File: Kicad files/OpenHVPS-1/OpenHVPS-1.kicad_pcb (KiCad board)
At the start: 2 copper layers, 77.5 x 20.5 mm, 71 parts, among them J1 Conn_01x03_Male, J2 Conn_01x03_Male, Q1 FQT7N10, Q2 BC846, Q3 MMDT3906, U1 74HC14, U2 MAX4162, U3 CD14538BM, U4 MAX6008AEUR+T

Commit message: cd \Users\allan\OneDrive\Documents\OpenHVPS  Please enter the commit message for your changes. Lines starting updated the long board design
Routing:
- net +3V3: track 0.00 -> 108.9 mm, vias 0 -> 2
- net Net-(Q1-Pad2): track 0.00 -> 57.3 mm, vias 0 -> 2
- net Net-(C14-Pad1): track 0.00 -> 53.8 mm, vias 0 -> 2
- net Net-(C16-Pad1): track 0.00 -> 49.5 mm, vias 0 -> 2
- net Net-(C19-Pad1): track 0.00 -> 47.4 mm, vias 0 -> 2
- net GND: track 0.00 -> 45.9 mm
- net Net-(H2-Pad1): track 0.00 -> 37.1 mm, vias 0 -> 1
- net Net-(Q2-Pad1): track 0.00 -> 32.8 mm, vias 0 -> 2
- net Net-(D9-Pad2): track 0.00 -> 32.4 mm
- net Net-(Q3-Pad1): track 0.00 -> 28.1 mm, vias 0 -> 2
- net Net-(C21-Pad1): track 0.00 -> 27.9 mm, vias 0 -> 3
- net Net-(D9-Pad1): track 0.00 -> 23.2 mm, vias 0 -> 2
- net Net-(D8-Pad2): track 0.00 -> 22.8 mm, vias 0 -> 2
- net Net-(C15-Pad1): track 0.00 -> 22.8 mm, vias 0 -> 2
- net +2V5: track 0.00 -> 22.6 mm, vias 0 -> 3
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
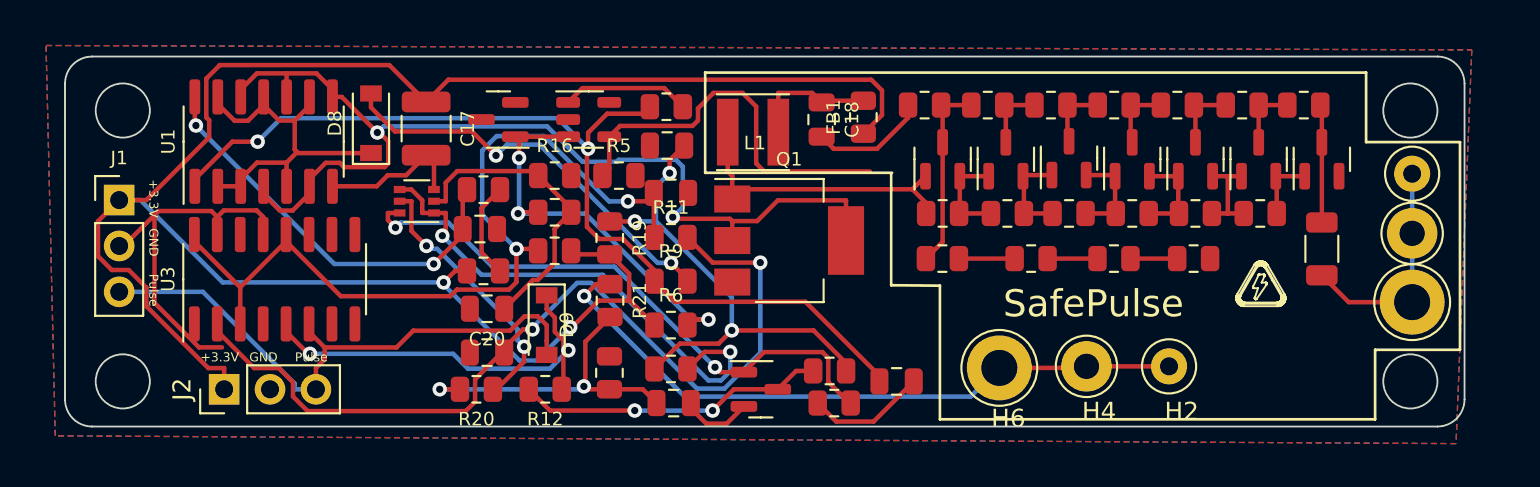
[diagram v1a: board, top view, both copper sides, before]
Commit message: changes to anode and cathode plus some parts layout, not routed!
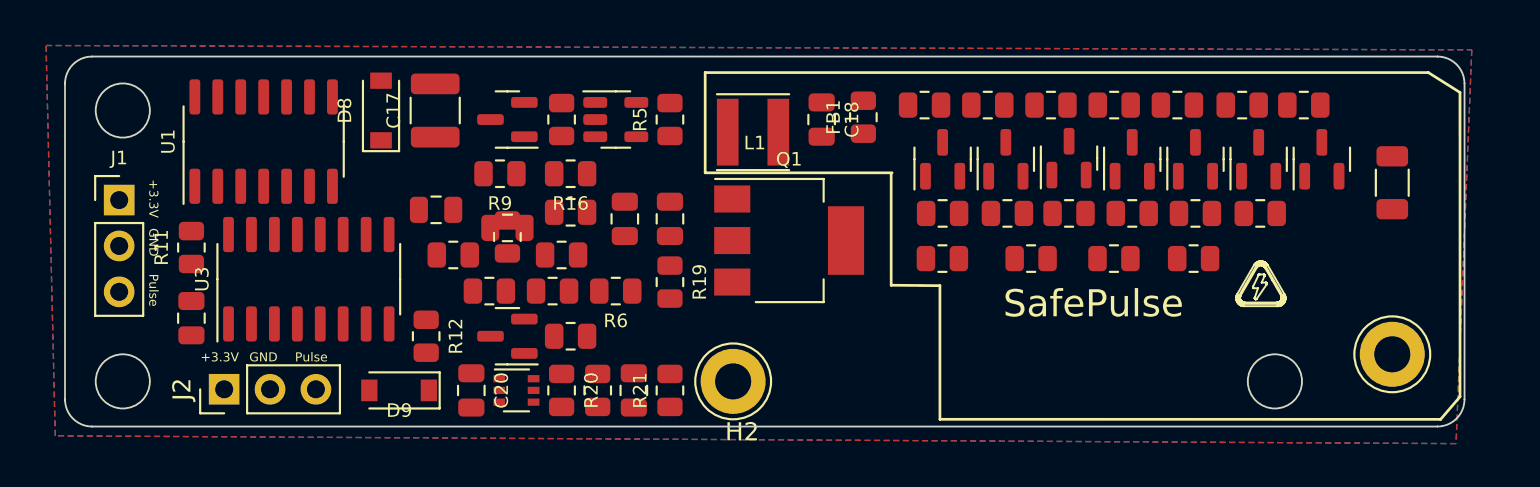
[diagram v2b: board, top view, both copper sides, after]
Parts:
- removed H1: A-1, TestPoint:TestPoint_Loop_D1.80mm_Drill1.0mm_Beaded
- removed H3: A-2, TestPoint:TestPoint_Loop_D2.60mm_Drill1.4mm_Beaded
- removed H4: C-2, TestPoint:TestPoint_Loop_D2.60mm_Drill1.4mm_Beaded
- removed H6: C-3, TestPoint:TestPoint_Loop_D3.80mm_Drill2.0mm
- H2: value C-1 -> Cathode; footprint TestPoint:TestPoint_Loop_D1.80mm_Drill1.0mm_Beaded -> TestPoint:TestPoint_Loop_D3.80mm_Drill2.0mm
- H5: value A-3 -> Anode
- moved R11 26.6 mm to (97.5, 67.6), turned to 90 degrees
- moved H2 24.2 mm to (127.5, 75.0)
- moved C14 23.2 mm to (115.0, 66.5)
- moved R14 21.8 mm to (112.0, 68.0)
- moved C16 16.5 mm to (97.5, 71.5), turned to -90 degrees
- moved R17 15.1 mm to (118.5, 72.5), turned to 0 degrees
- moved Q2 14.3 mm to (115.0, 72.5), turned to 180 degrees
- moved Q3 11.8 mm to (115.5, 75.5), turned to 0 degrees
- moved R9 11.2 mm to (114.6, 63.5), turned to 180 degrees
- moved R18 10.9 mm to (114.0, 70.0)
- moved D9 8.94 mm to (109.0, 75.5), turned to 180 degrees
- moved R12 7.22 mm to (110.5, 72.5), turned to -90 degrees
- moved R21 5.98 mm to (124.0, 75.5), turned to 90 degrees
- moved R8 5.84 mm to (118.0, 60.5), turned to 90 degrees
- moved R7 5.35 mm to (164.0, 64.0)
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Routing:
- net +3V3: track 108.9 -> 0.00 mm, vias 2 -> 0
- net Net-(Q1-Pad2): track 57.3 -> 0.00 mm, vias 2 -> 0
- net Net-(C14-Pad1): track 53.8 -> 0.00 mm, vias 2 -> 0
- net Net-(C16-Pad1): track 49.5 -> 0.00 mm, vias 2 -> 0
- net Net-(C19-Pad1): track 47.4 -> 0.00 mm, vias 2 -> 0
- net GND: track 45.9 -> 0.00 mm
- net Net-(H2-Pad1): track 37.1 -> 0.00 mm, vias 1 -> 0
- net Net-(Q2-Pad1): track 32.8 -> 0.00 mm, vias 2 -> 0
- net Net-(D9-Pad2): track 32.4 -> 0.00 mm
- net Net-(Q3-Pad1): track 28.1 -> 0.00 mm, vias 2 -> 0
- net Net-(C21-Pad1): track 27.9 -> 0.00 mm, vias 3 -> 0
- net Net-(D9-Pad1): track 23.2 -> 0.00 mm, vias 2 -> 0
- net Net-(D8-Pad2): track 22.8 -> 0.00 mm, vias 2 -> 0
- net Net-(C15-Pad1): track 22.8 -> 0.00 mm, vias 2 -> 0
- net +2V5: track 22.6 -> 0.00 mm, vias 3 -> 0
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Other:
- outline, holes or cut-outs redrawn

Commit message: Routed the board
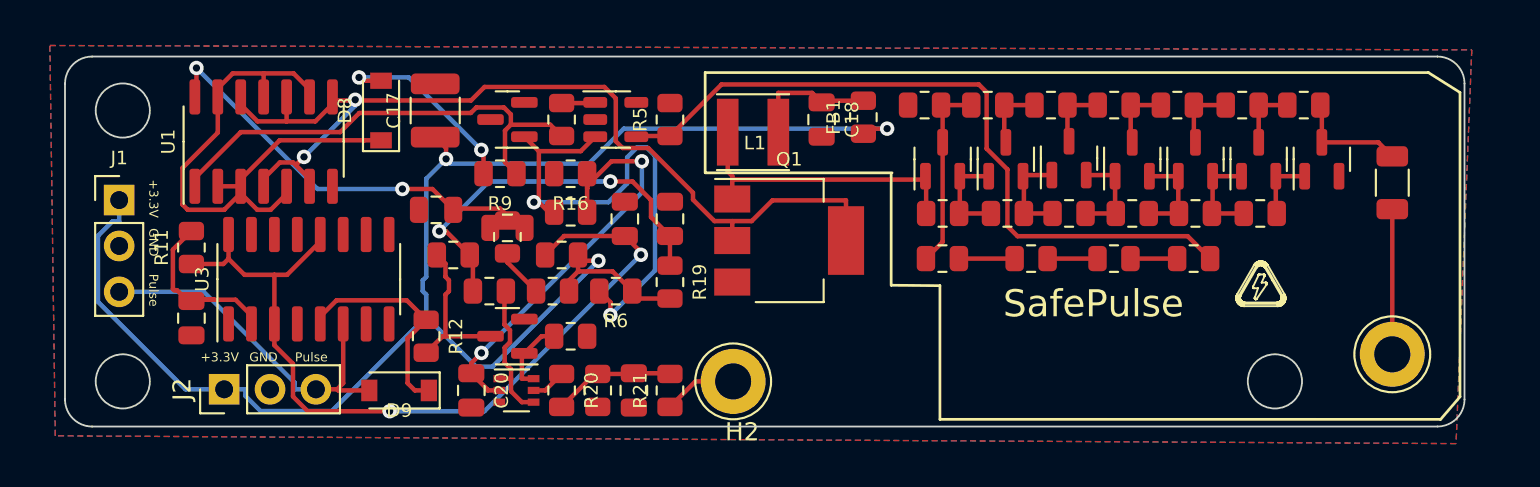
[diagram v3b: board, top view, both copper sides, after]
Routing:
- net +3V3: track 0.00 -> 89.1 mm, vias 0 -> 3
- net Net-(Q1-Pad2): track 0.00 -> 54.4 mm, vias 0 -> 2
- net Net-(C19-Pad1): track 0.00 -> 46.7 mm, vias 0 -> 2
- net Net-(R4-Pad1): track 0.00 -> 40.6 mm
- net Net-(D8-Pad1): track 0.00 -> 32.9 mm
- net +2V5: track 0.00 -> 29.2 mm, vias 0 -> 2
- net Net-(C14-Pad1): track 0.00 -> 26.5 mm
- net Net-(C20-Pad1): track 0.00 -> 23.5 mm, vias 0 -> 2
- net Net-(C15-Pad1): track 0.00 -> 22.6 mm, vias 0 -> 2
- net Net-(C21-Pad1): track 0.00 -> 21.7 mm, vias 0 -> 2
- net Net-(D9-Pad2): track 0.00 -> 20.1 mm
- net Net-(C2-Pad1): track 0.00 -> 16.5 mm
- net Net-(D9-Pad1): track 0.00 -> 12.4 mm
- net Net-(D8-Pad2): track 0.00 -> 11.1 mm, vias 0 -> 2
- net Net-(C1-Pad2): track 0.00 -> 10.6 mm
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
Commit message: Changed foot prints for Anade/Cathode
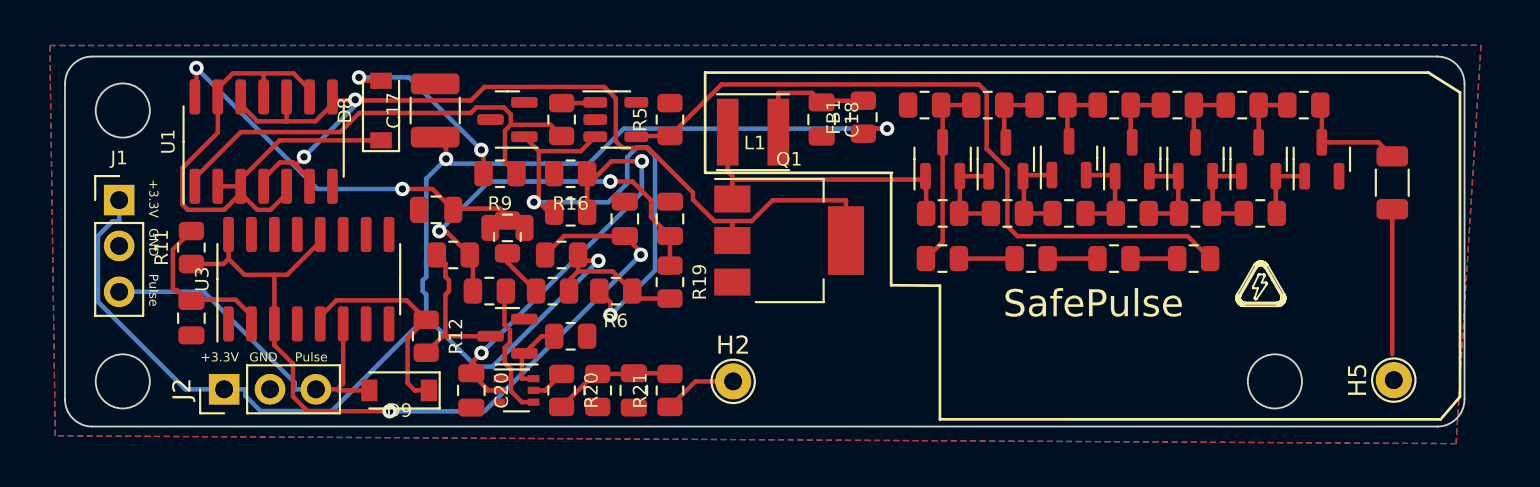
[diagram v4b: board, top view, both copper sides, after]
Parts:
- H2, H5: footprint TestPoint:TestPoint_Loop_D3.80mm_Drill2.0mm -> TestPoint:TestPoint_THTPad_D2.0mm_Drill1.0mm
- moved H5 1.43 mm to (164.1, 74.9)
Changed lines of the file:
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@@
       (net 24 "Net-(D9-Pad2)") (pinfunction "Pin_3"))
     (model "${KICAD6_3DMODEL_DIR}/Connector_PinHeader_2.54mm.3dshapes/PinHeader_1x03_P2.54mm_Vertical.wrl"
-      (offset (xyz 0 0 0))
+      (offset (xyz 0 0 -2))
       (scale (xyz 1 1 1))
-      (rotate (xyz 0 0 0))
+      (rotate (xyz 0 -180 0))
     )
   )
-  (footprint "TestPoint:TestPoint_Loop_D3.80mm_Drill2.0mm" (layer "F.Cu")
-    (at 164 73.5 90)
-    (descr "wire loop as test point, loop diameter 3.8mm, hole diameter 2.0mm")
-    (tags "test point wire loop bead")
+  (footprint "TestPoint:TestPoint_THTPad_D2.0mm_Drill1.0mm" (layer "F.Cu")
+    (at 164.084 74.93 90)
+    (descr "THT pad as test Point, diameter 2.0mm, hole diameter 1.0mm")
+    (tags "test point THT pad")
     (property "Sheet file" "OpenHVPS-1.kicad_sch")
     (property "Sheet name" "")
-    (attr through_hole)
-    (fp_text reference "H5" (at 0.5 2.8 90) (layer "F.SilkS") hide
+    (attr exclude_from_pos_files exclude_from_bom)
+    (fp_text reference "H5" (at 0 -1.998 90) (layer "F.SilkS")
       (effects (font (size 1 1) (thickness 0.15)))
     )
-    (fp_text value "Anode" (at 0 -2.8 90) (layer "F.Fab")
+    (fp_text value "Anode" (at 0 2.05 90) (layer "F.Fab")
       (effects (font (size 1 1) (thickness 0.15)))
     )
-    (fp_text user "${REFERENCE}" (at 0.5 2.8 90) (layer "F.Fab") hide
+    (fp_text user "${REFERENCE}" (at 0 -2 90) (layer "F.Fab")
       (effects (font (size 1 1) (thickness 0.15)))
     )
-    (fp_circle (center 0 0) (end 2.1 0) (layer "F.SilkS") (width 0.12) (fill none))
-    (fp_circle (center 0 0) (end 2.3 0) (layer "F.CrtYd") (width 0.05) (fill none))
-    (fp_line (start 1.9 0.3) (end 1.9 -0.3) (layer "F.Fab") (width 0.12))
-    (fp_line (start 1.9 -0.3) (end -1.9 -0.3) (layer "F.Fab") (width 0.12))
-    (fp_line (start -1.9 -0.3) (end -1.9 0.3) (layer "F.Fab") (width 0.12))
-    (fp_line (start -1.9 0.3) (end 1.9 0.3) (layer "F.Fab") (width 0.12))
-    (pad "1" thru_hole circle (at 0 0 90) (locked) (size 3.6 3.6) (drill 2) (layers *.Cu *.Mask)
+    (fp_circle (center 0 0) (end 0 1.2) (layer "F.SilkS") (width 0.12) (fill none))
+    (fp_circle (center 0 0) (end 1.5 0) (layer "F.CrtYd") (width 0.05) (fill none))
+    (pad "1" thru_hole circle (at 0 0 90) (locked) (size 2 2) (drill 1) (layers *.Cu *.Mask)
       (net 49 "Net-(H5-Pad1)") (pinfunction "1"))
-    (model "${KICAD6_3DMODEL_DIR}/TestPoint.3dshapes/TestPoint_Loop_D3.80mm_Drill2.0mm.wrl"
-      (offset (xyz 0 0 0))
-      (scale (xyz 1 1 1))
-      (rotate (xyz 0 0 0))
-    )
   )
   (footprint "Package_TO_SOT_SMD:SOT-23" (layer "F.Cu")
@@
     )
   )
-  (footprint "TestPoint:TestPoint_Loop_D3.80mm_Drill2.0mm" (layer "F.Cu")
+  (footprint "TestPoint:TestPoint_THTPad_D2.0mm_Drill1.0mm" (layer "F.Cu")
     (at 127.5 75)
-    (descr "wire loop as test point, loop diameter 3.8mm, hole diameter 2.0mm")
-    (tags "test point wire loop bead")
+    (descr "THT pad as test Point, diameter 2.0mm, hole diameter 1.0mm")
+    (tags "test point THT pad")
     (property "Sheet file" "OpenHVPS-1.kicad_sch")
     (property "Sheet name" "")
-    (attr through_hole)
-    (fp_text reference "H2" (at 0.5 2.8) (layer "F.SilkS")
+    (attr exclude_from_pos_files exclude_from_bom)
+    (fp_text reference "H2" (at 0 -1.998) (layer "F.SilkS")
       (effects (font (size 1 1) (thickness 0.15)))
     )
-    (fp_text value "Cathode" (at 0 -2.8) (layer "F.Fab")
+    (fp_text value "Cathode" (at 0 2.05) (layer "F.Fab")
       (effects (font (size 1 1) (thickness 0.15)))
     )
-    (fp_text user "${REFERENCE}" (at 0.5 2.8) (layer "F.Fab")
+    (fp_text user "${REFERENCE}" (at 0 -2) (layer "F.Fab")
       (effects (font (size 1 1) (thickness 0.15)))
     )
-    (fp_circle (center 0 0) (end 2.1 0) (layer "F.SilkS") (width 0.12) (fill none))
-    (fp_circle (center 0 0) (end 2.3 0) (layer "F.CrtYd") (width 0.05) (fill none))
-    (fp_line (start -1.9 0.3) (end 1.9 0.3) (layer "F.Fab") (width 0.12))
-    (fp_line (start 1.9 -0.3) (end -1.9 -0.3) (layer "F.Fab") (width 0.12))
-    (fp_line (start -1.9 -0.3) (end -1.9 0.3) (layer "F.Fab") (width 0.12))
-    (fp_line (start 1.9 0.3) (end 1.9 -0.3) (layer "F.Fab") (width 0.12))
-    (pad "1" thru_hole circle (at 0 0) (locked) (size 3.6 3.6) (drill 2) (layers *.Cu *.Mask)
+    (fp_circle (center 0 0) (end 0 1.2) (layer "F.SilkS") (width 0.12) (fill none))
+    (fp_circle (center 0 0) (end 1.5 0) (layer "F.CrtYd") (width 0.05) (fill none))
+    (pad "1" thru_hole circle (at 0 0) (locked) (size 2 2) (drill 1) (layers *.Cu *.Mask)
       (net 48 "Net-(H2-Pad1)") (pinfunction "1"))
-    (model "${KICAD6_3DMODEL_DIR}/TestPoint.3dshapes/TestPoint_Loop_D3.80mm_Drill2.0mm.wrl"
-      (offset (xyz 0 0 0))
-      (scale (xyz 1 1 1))
-      (rotate (xyz 0 0 0))
-    )
   )
   (footprint "Package_TO_SOT_SMD:SOT-23-5" (layer "F.Cu")
@@
       (effects (font (size 0.75 0.75) (thickness 0.1)))
     )
-    (fp_text value "FQT7N10" (at 0 4.5) (layer "F.Fab")
+    (fp_text value "FQT7N10" (at 0 4.5) (layer "F.Fab") hide
       (effects (font (size 0.75 0.75) (thickness 0.1)))
     )
@@
         (xy 89.959933 78.015183)
         (xy 89.662 56.4)
-        (xy 168.402 56.642)
+        (xy 168.91 56.388)
       )
     )
